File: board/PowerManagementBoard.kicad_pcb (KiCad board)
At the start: 2 copper layers, 168 parts, among them IC1 ACS37010LLZATR-030B3, IC2 ACS37010LLZATR-030B3, IC3 ACS37010LLZATR-030B3, IC4 ACS37010LLZATR-030B3, IC5 ACS37010LLZATR-030B3, IC6 ACS37010LLZATR-030B3, J1 RJ45_LED_Shielded, J10 768250002, J11 768250002, J12 768250002, J2 SS-73100-082, J3 SS-73100-082, J4 SS-73100-082, J5 768250002, J6 768250002, J7 768250002, J8 768250002, J9 768250002, Q1 BSS138, Q10 Si4162DY, Q2 IPB180N10S4-02, Q3 Si4162DY, Q4 IPB180N10S4-02, Q5 Si4162DY, Q6 Si4162DY, Q7 Si4162DY, Q8 Si4162DY, Q9 IPB180N10S4-02, U1 LT1910, U10 ACS72981LLRATR-100U3, U11 LT1910, U12 LT1910, U13 LT1910, U14 LT1910, U15 Teensy4.1_DEV-16771, U16 OKI-78SR-3.3_1.5-W36H-C, U17 OKI-78SR-5_1.5-W36H-C, U18 Opamp_Dual, U19 LT1910, U2 LM5050MK-1_NOPB, U20 LT1910, U3 LM5050MK-1_NOPB, U4 Opamp_Dual, U5 Opamp_Dual, U6 Opamp_Dual

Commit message: PCB start
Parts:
- moved Conn2 36.0 mm to (76.1, 168.5)
- moved Q2 27.7 mm to (95.0, 162.6)
- moved J5 6.38 mm to (20.9, 128.0)
- moved J10 6.38 mm to (64.8, 102.2)
- moved J12 6.38 mm to (86.8, 102.2)
- moved J6 6.38 mm to (20.9, 102.2)
- moved J9 6.38 mm to (53.8, 102.2)
- moved J7 6.38 mm to (31.9, 102.2)
- moved J8 6.38 mm to (42.9, 102.2)
- moved J11 6.38 mm to (75.8, 102.2)
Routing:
- net /TeensyandEthernetCircuit/LED: track 0.00 -> 79.8 mm

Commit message: designated an area for each circuit on pcb
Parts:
- removed the U5 at (122.9, 29.5)
- moved R51 258.9 mm to (67.7, 167.2)
- moved R52 258.9 mm to (67.7, 169.8)
- moved R53 257.6 mm to (44.3, 129.5), turned to 90 degrees
- moved R54 255.5 mm to (46.3, 131.3), turned to -90 degrees
- moved C17 255.4 mm to (44.1, 141.6)
- moved R49 255.1 mm to (44.1, 139.8)
- moved R50 251.7 mm to (47.0, 140.7), turned to -90 degrees
- moved C23 249.7 mm to (43.3, 132.2)
- moved D2 247.1 mm to (44.7, 190.3)
- moved D3 247.1 mm to (44.7, 194.9)
- moved Q9 246.1 mm to (51.4, 181.9)
- moved C18 246.0 mm to (67.7, 164.7)
- moved U3 240.6 mm to (60.2, 190.3)
- moved V3 238.5 mm to (22.5, 185.4), turned to 90 degrees
- moved R42 237.4 mm to (91.8, 168.9)
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- renumbered U18 to U5
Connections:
- net /Anderson/Cam1 renamed /LC
- U5 pad 4: (no net) -> GND
- U5 pad 5: (no net) -> Net-(U5B-+)
- U5 pad 6: (no net) -> Net-(U5B--)
- U5 pad 7: (no net) -> Net-(R22-Pad1)
- U5 pad 8: (no net) -> +24V
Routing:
- net /TeensyandEthernetCircuit/RX+: track 58.3 -> 99.6 mm
- net /TeensyandEthernetCircuit/TX+: track 60.6 -> 101.5 mm
- net /TeensyandEthernetCircuit/RX-: track 61.0 -> 95.8 mm
- net /TeensyandEthernetCircuit/TX-: track 67.5 -> 101.9 mm
- net /TeensyandEthernetCircuit/LED: track 79.8 -> 114.1 mm
- net GND: track 0.00 -> 17.6 mm
- net Net-(D4-K): track 0.00 -> 16.6 mm
- net Net-(IC1-VREF): track 0.00 -> 6.29 mm
- net +3V3: track 0.00 -> 1.86 mm
- added copper zone on F.Cu, net /LC

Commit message: Configuration of parts
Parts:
- moved R27 83.1 mm to (192.8, 108.4), turned to 180 degrees
- moved D6 63.3 mm to (188.8, 108.6)
- moved R11 39.4 mm to (206.2, 137.7)
- moved R10 37.6 mm to (211.7, 133.6), turned to 0 degrees
- moved U6 36.2 mm to (201.5, 133.0), turned to 0 degrees
- moved R19 33.4 mm to (219.9, 112.2), turned to 0 degrees
- moved R9 31.2 mm to (219.8, 117.1), turned to 0 degrees
- moved IC6 30.5 mm to (51.3, 147.3), turned to 180 degrees
- moved R52 29.1 mm to (45.7, 150.7), turned to -90 degrees
- moved R24 26.6 mm to (219.8, 104.6), turned to 0 degrees
- moved R12 25.1 mm to (206.1, 132.8)
- moved D8 25.0 mm to (181.7, 105.4), turned to 180 degrees
- moved R51 24.7 mm to (49.2, 150.9), turned to 180 degrees
- moved R13 21.3 mm to (201.5, 129.1), turned to 0 degrees
- moved U5 21.3 mm to (198.4, 118.3), turned to 0 degrees
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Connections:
- R3 pad 1: +3.3V -> +3V3
- R35 pad 1: +3.3V -> +3V3
- R36 pad 1: +3.3V -> +3V3
- R37 pad 1: +3.3V -> +3V3
- R38 pad 1: +3.3V -> +3V3
- R44 pad 1: +3.3V -> +3V3
- R45 pad 1: +3.3V -> +3V3
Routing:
- net +3V3: track 1.86 -> 86.8 mm
- net +5V: track 0.00 -> 8.00 mm
- net Net-(IC6-VREF): track 0.00 -> 4.79 mm
- net Net-(D23-A): track 0.00 -> 2.55 mm
- net Net-(D22-A): track 0.00 -> 2.55 mm
- net Net-(U13-FAULT): track 0.00 -> 2.52 mm
- net Net-(D18-A): track 0.00 -> 2.45 mm

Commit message: Rearrangement #2
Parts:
- added C13: 1000uF, Capacitor_THT:CP_Radial_D16.0mm_P7.50mm, F.Cu at (40.4, 25.9)
- added C24: 1000uF, Capacitor_THT:CP_Radial_D16.0mm_P7.50mm, F.Cu at (22.6, 48.3)
- added C4: 1000uF, Capacitor_THT:CP_Radial_D16.0mm_P7.50mm, F.Cu at (40.6, 47.6)
- Conn1: footprint MRDT_Connectors:MOLEX_SL_07_Horizontal -> MRDT_Connectors:MOLEX_SL_07_Vertical
- moved Conn1 157.4 mm to (72.2, 67.1), turned to 0 degrees
- moved R24 150.5 mm to (72.3, 74.9), turned to 90 degrees
- moved R4 148.6 mm to (74.9, 74.8), turned to 90 degrees
- moved R14 146.6 mm to (77.5, 74.8), turned to 90 degrees
- moved R19 144.9 mm to (79.9, 74.8), turned to 90 degrees
- moved R30 143.0 mm to (82.5, 74.9), turned to 90 degrees
- moved Conn2 142.7 mm to (135.5, 52.6), turned to -90 degrees
- moved R9 141.5 mm to (84.8, 74.9), turned to 90 degrees
- moved R16 137.9 mm to (70.8, 87.0), turned to 90 degrees
- moved R15 136.4 mm to (72.5, 87.0), turned to 90 degrees
- moved R18 134.8 mm to (74.3, 87.1), turned to 90 degrees
- moved R56 134.5 mm to (124.1, 61.8), turned to -90 degrees
- moved LCD1 134.4 mm to (93.0, 98.4), turned to 180 degrees
- moved R17 131.9 mm to (73.3, 90.4), turned to 180 degrees
- moved C9 131.4 mm to (15.4, 140.8), turned to 180 degrees
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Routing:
- net /TeensyandEthernetCircuit/LED: track 114.1 -> 0.00 mm
- net /TeensyandEthernetCircuit/TX-: track 101.9 -> 0.00 mm
- net /TeensyandEthernetCircuit/TX+: track 101.5 -> 0.00 mm
- net /TeensyandEthernetCircuit/RX+: track 99.6 -> 0.00 mm
- net /TeensyandEthernetCircuit/RX-: track 95.8 -> 0.00 mm
- net +3V3: track 86.8 -> 0.07 mm
- net Net-(D4-K): track 16.6 -> 0.00 mm
- net Net-(C9-Pad1): track 15.3 -> 0.00 mm
- net +5V: track 8.00 -> 0.07 mm
- net Net-(IC1-VREF): track 6.29 -> 0.00 mm
- net Net-(IC6-VREF): track 4.79 -> 0.00 mm
- net Net-(D22-A): track 2.55 -> 0.01 mm
- net Net-(D23-A): track 2.55 -> 0.01 mm
- net Net-(D18-A): track 2.45 -> 0.00 mm

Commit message: Board before M5 Kill
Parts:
- removed Conn2: AndersonPP, MRDT_Connectors:Square_Anderson_2_H_Side_By_Side_PV
- added J13: 768250002, PowerManagementBoard:CONN_SD-76825-0100_02_MOL, F.Cu at (179.4, 40.3)
- added J14: 768250002, PowerManagementBoard:CONN_SD-76825-0100_02_MOL, F.Cu at (168.4, 40.3)
- added J15: 768250002, PowerManagementBoard:CONN_SD-76825-0100_02_MOL, F.Cu at (157.4, 40.3)
- added J16: 768250002, PowerManagementBoard:CONN_SD-76825-0100_02_MOL, F.Cu at (72.3, 40.7)
- added J17: 768250002, PowerManagementBoard:CONN_SD-76825-0100_02_MOL, F.Cu at (61.3, 40.7)
- added J18: 768250002, PowerManagementBoard:CONN_SD-76825-0100_02_MOL, F.Cu at (50.3, 40.7)
- moved H1 231.0 mm to (197.8, 150.7)
- moved H4 196.2 mm to (198.2, 36.6)
- moved J7 182.5 mm to (190.1, 58.6), turned to 90 degrees
- moved J5 181.4 mm to (190.0, 48.6), turned to 90 degrees
- moved R49 172.5 mm to (183.3, 55.2), turned to 180 degrees
- moved C17 172.3 mm to (183.3, 53.4), turned to 180 degrees
- moved R50 168.3 mm to (180.4, 54.3), turned to 90 degrees
- moved D1 165.6 mm to (193.7, 139.8)
- moved Q1 165.6 mm to (192.9, 142.9)
- moved R34 165.6 mm to (193.6, 137.8)
- moved B1 165.6 mm to (185.6, 135.1)
- moved IC3 164.5 mm to (177.3, 58.7), turned to 0 degrees
- moved C9 162.1 mm to (177.0, 128.0), turned to -90 degrees
- moved R37 162.0 mm to (178.9, 48.6), turned to 180 degrees
- moved Q5 158.7 mm to (174.5, 53.1), turned to 180 degrees
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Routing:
- net GND: track 17.6 -> 0.07 mm
- net Net-(D2-K): track 0.00 -> 3.62 mm
- net Net-(U13-FAULT): track 2.52 -> 0.08 mm
- net +24V: track 0.00 -> 2.24 mm
- net Net-(Q2-G): vias 0 -> 1
- net /Anderson/Motor: vias 0 -> 5
- added copper zone on F.Cu, net +24V
- added copper zone on B.Cu, net /Anderson/Motor
- added copper zone on F.Cu, net GND
- added copper zone on F.Cu, net Net-(D14-K)

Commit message: Planned layout - before wiring.
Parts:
- removed C16: 0.1uF, Capacitor_SMD:C_0603_1608Metric_Pad1.08x0.95mm_HandSolder
- removed C22: 10uF, Capacitor_SMD:C_0603_1608Metric_Pad1.08x0.95mm_HandSolder
- removed D17, D19: GRN, LED_SMD:LED_0603_1608Metric_Pad1.05x0.95mm_HandSolder
- removed IC5: ACS37010LLZATR-030B3, PowerManagementBoard:IC_ACS37030LLZATR-040B3
- removed J4: SS-73100-082, PowerManagementBoard:BEL_SS-73100-082
- removed Q10: Si4162DY, Package_SO:SOIC-8_3.9x4.9mm_P1.27mm
- removed R45: 5.1k, Resistor_SMD:R_0603_1608Metric_Pad0.98x0.95mm_HandSolder
- removed R47, R48: 10k, Resistor_SMD:R_0603_1608Metric_Pad0.98x0.95mm_HandSolder
- removed R57, R59: 6.8k, Resistor_SMD:R_0603_1608Metric_Pad0.98x0.95mm_HandSolder
- removed U20: LT1910, Package_SO:SOIC-8_3.9x4.9mm_P1.27mm
- moved C26 95.0 mm to (87.9, 141.8)
- moved C25 95.0 mm to (85.4, 141.8)
- moved D23 95.0 mm to (92.9, 141.8)
- moved R63 95.0 mm to (90.4, 141.8)
- moved U17 95.0 mm to (86.6, 123.8)
- moved U12 79.1 mm to (92.9, 53.1)
- moved R36 78.9 mm to (93.6, 59.1)
- moved R60 78.9 mm to (86.7, 59.5)
- moved C6 78.3 mm to (92.9, 48.4)
- moved D20 78.1 mm to (89.3, 59.5)
- moved Q7 75.7 mm to (86.2, 53.1), turned to 90 degrees
- moved C19 73.9 mm to (99.0, 142.0)
- moved C20 73.9 mm to (101.5, 142.0)
- moved D22 73.9 mm to (105.9, 141.9)
- moved U16 73.9 mm to (99.6, 123.6)
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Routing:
- net Net-(D14-K): track 0.00 -> 40.7 mm
- net Net-(D2-K): track 3.62 -> 0.00 mm
- net +24V: track 2.24 -> 0.00 mm
- net Net-(Q2-G): vias 1 -> 0
- added copper zone on B.Cu, net GND
- added copper zone on F.Cu, net Net-(D2-K)
- added copper zone on F.Cu, net Net-(D4-K)

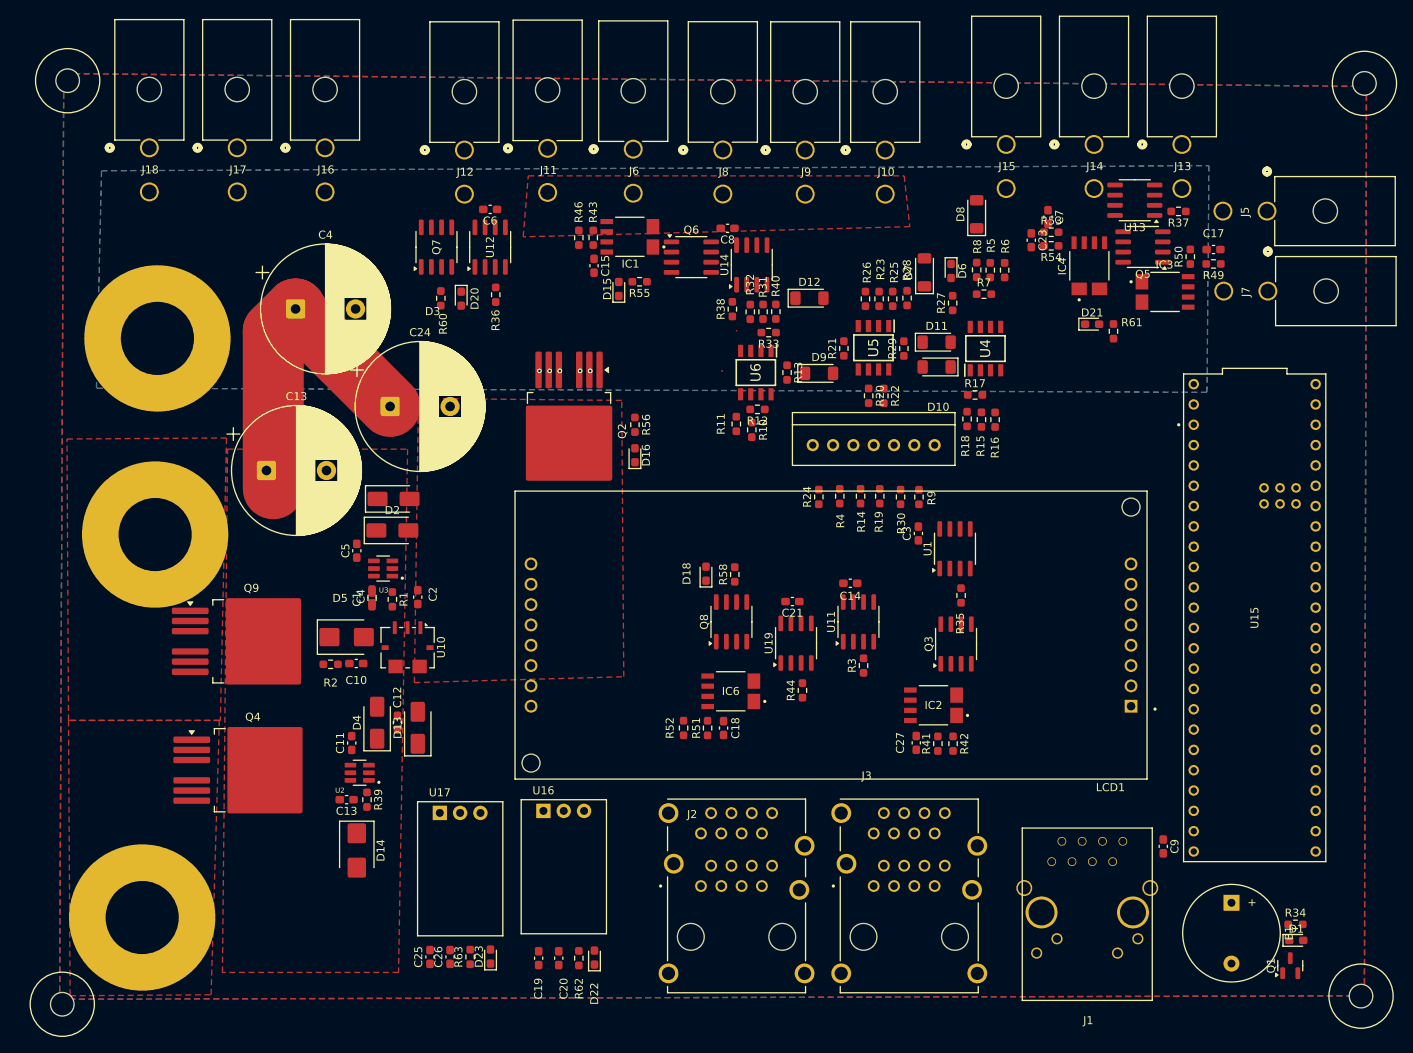
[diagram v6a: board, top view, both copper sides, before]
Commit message: added edge cuts
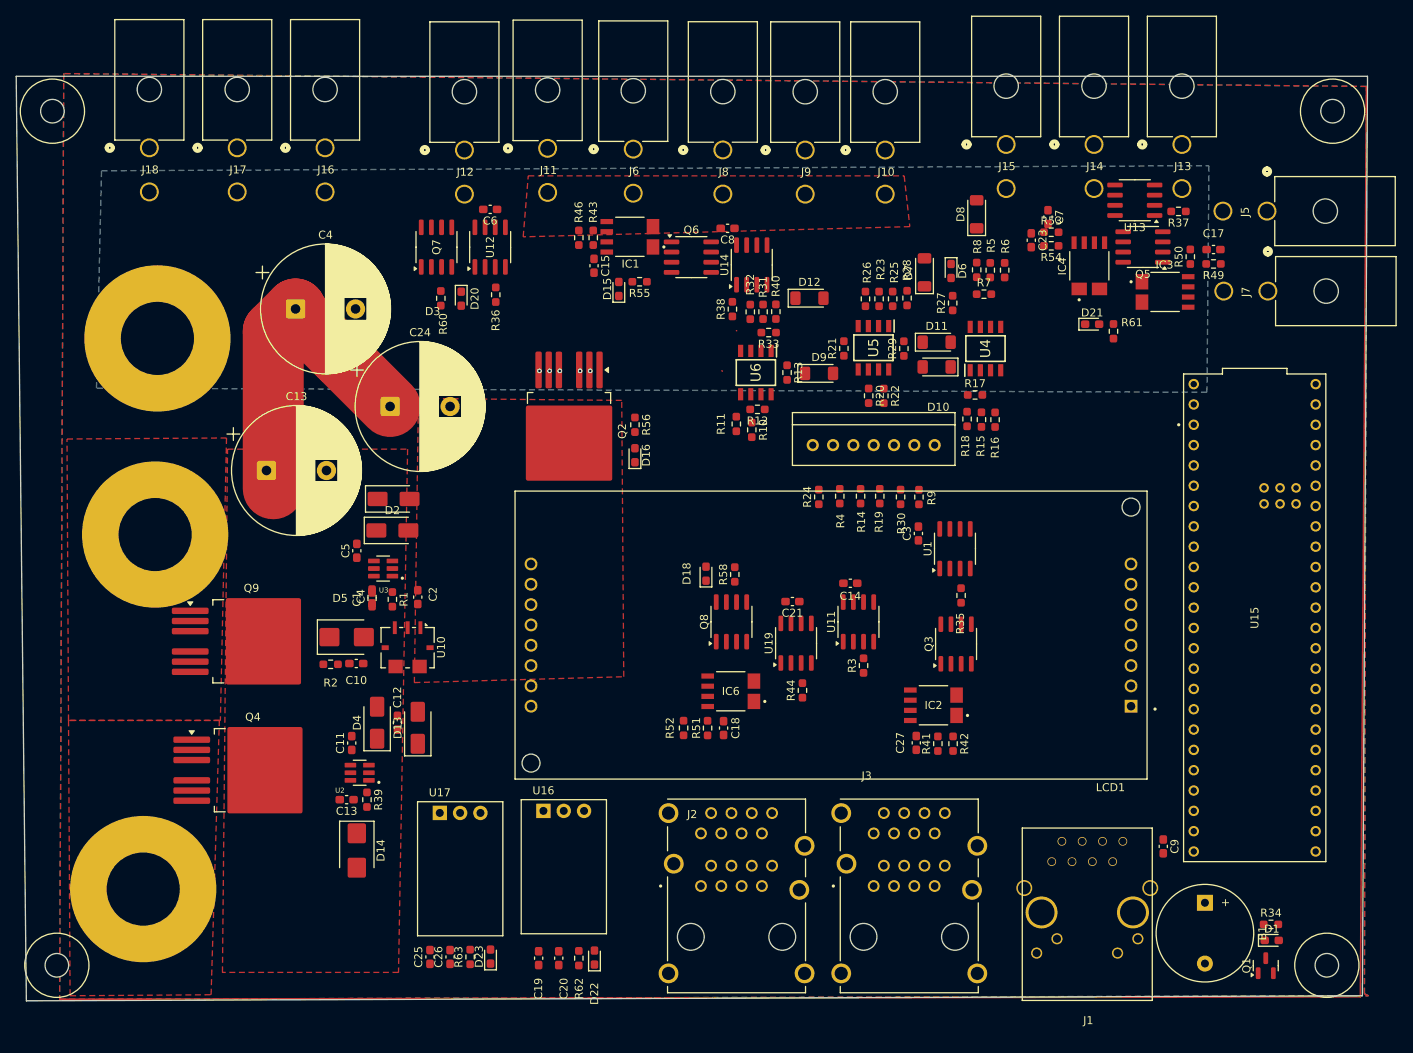
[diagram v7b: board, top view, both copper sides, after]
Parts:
- moved H1 5.75 mm to (193.5, 146.9)
- moved H4 5.28 mm to (194.2, 40.1)
- moved H2 4.92 mm to (42.7, 146.9)
- moved H3 4.26 mm to (34.2, 40.1)
- moved V1 3.56 mm to (49.5, 133.3)
- moved B1 3.32 mm to (182.2, 135.1)
- moved D1 3.06 mm to (190.6, 139.8)
- moved Q1 3.06 mm to (189.8, 142.9)
- moved R34 3.06 mm to (190.5, 137.8)
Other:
- board outline added: 168.9 x 115.6 mm
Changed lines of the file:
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@@
 	(footprint "Resistor_SMD:R_0603_1608Metric_Pad0.98x0.95mm_HandSolder"
 		(layer "F.Cu")
-		(at 193.563 137.761)
+		(at 190.5 137.761)
 		(descr "Resistor SMD 0603 (1608 Metric), square (rectangular) end terminal, IPC-7351 nominal with elongated pad for handsoldering. (Body size source: IPC-SM-782 page 72, https://www.pcb-3d.com/wordpress/wp-content/uploads/ipc-sm-782a_amendment_1_and_2.pdf), generated with kicad-footprint-generator")
 		(tags "resistor handsolder")
@@
 	(footprint "MRDT_Drill_Holes:4_40_Hole_Corner"
 		(layer "F.Cu")
-		(at 197.7503 150.7377)
+		(at 193.47688 146.88312)
 		(property "Reference" "H1"
 			(at 4.00812 -3.50812 0)
@@
 	(footprint "MRDT_Drill_Holes:4_40_Hole_Corner"
 		(layer "F.Cu")
-		(at 36.0793 36.3107)
+		(at 34.1743 40.1207)
 		(property "Reference" "H3"
 			(at 4.00812 -3.50812 0)
@@
 	(footprint "LED_SMD:LED_0603_1608Metric_Pad1.05x0.95mm_HandSolder"
 		(layer "F.Cu")
-		(at 193.663 139.761)
+		(at 190.6 139.761)
 		(descr "LED SMD 0603 (1608 Metric), square (rectangular) end terminal, IPC-7351 nominal, (Body size source: http://www.tortai-tech.com/upload/download/2011102023233369053.pdf), generated with kicad-footprint-generator")
 		(tags "LED handsolder")
@@
 	(footprint "Package_TO_SOT_SMD:SOT-23"
 		(layer "F.Cu")
-		(at 192.913 142.9235 90)
+		(at 189.85 142.9235 90)
 		(descr "SOT, 3 Pin (JEDEC TO-236 Var AB https://www.jedec.org/document_search?search_api_views_fulltext=TO-236), generated with kicad-footprint-generator ipc_gullwing_generator.py")
 		(tags "SOT TO_SOT_SMD")
@@
 	(footprint "MRDT_Drill_Holes:4_40_Hole_Corner"
 		(layer "F.Cu")
-		(at 43.4227 151.7537 90)
+		(at 42.74312 146.88312 90)
 		(property "Reference" "H2"
 			(at 4.00812 -3.50812 90)
@@
 	(footprint "Buzzer_Beeper:Buzzer_12x9.5RM7.6"
 		(layer "F.Cu")
-		(at 185.563 135.061 -90)
+		(at 182.245 135.061 -90)
 		(descr "Generic Buzzer, D12mm height 9.5mm with RM7.6mm")
 		(tags "buzzer")
@@
 	(footprint "MRDT_Drill_Holes:BATT_PWR_VIA"
 		(layer "F.Cu")
-		(at 49.403 136.906 180)
+		(at 49.53 133.35 180)
 		(property "Reference" "V1"
 			(at 0 10.16 0)
@@
 	(footprint "MRDT_Drill_Holes:4_40_Hole_Corner"
 		(layer "F.Cu")
-		(at 198.17588 36.64712)
+		(at 194.1943 40.1207)
 		(property "Reference" "H4"
 			(at 4.00812 -3.50812 0)
@@
 		)
 	)
+	(gr_line
+		(start 202.438 33.02)
+		(end 201.676 146.812)
+		(stroke
+			(width 0.2)
+			(type default)
+		)
+		(layer "F.Cu")
+	)
+	(gr_line
+		(start 201.676 146.812)
+		(end 39.087387 147.123226)
+		(stroke
+			(width 0.2)
+			(type default)
+		)
+		(layer "F.Cu")
+	)
+	(gr_line
+		(start 33.655 31.75)
+		(end 202.565 31.75)
+		(stroke
+			(width 0.05)
+			(type default)
+		)
+		(layer "Edge.Cuts")
+	)
+	(gr_line
+		(start 34.925 147.32)
+		(end 33.655 31.75)
+		(stroke
+			(width 0.05)
+			(type default)
+		)
+		(layer "Edge.Cuts")
+	)
+	(gr_line
+		(start 202.565 33.02)
+		(end 201.93 146.685)
+		(stroke
+			(width 0.05)
+			(type default)
+		)
+		(layer "Edge.Cuts")
+	)
+	(gr_line
+		(start 201.93 146.685)
+		(end 34.925 147.32)
+		(stroke
+			(width 0.05)
+			(type default)
+		)
+		(layer "Edge.Cuts")
+	)
+	(gr_line
+		(start 202.565 31.75)
+		(end 202.565 33.02)
+		(stroke
+			(width 0.05)
+			(type default)
+		)
+		(layer "Edge.Cuts")
+	)
 	(segment

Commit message: Most Traces done
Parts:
- moved R36 75.3 mm to (168.9, 60.6), turned to 180 degrees
- moved Q7 74.6 mm to (160.8, 55.6)
- moved U12 74.5 mm to (167.4, 55.6)
- moved C6 74.5 mm to (167.4, 50.7)
- moved D20 74.4 mm to (163.7, 60.8), turned to 180 degrees
- moved R60 73.2 mm to (159.9, 60.8), turned to 0 degrees
- moved J12 53.6 mm to (143.3, 40.6)
- moved J11 32.2 mm to (132.3, 40.6)
- moved J18 24.9 mm to (75.2, 40.6)
- moved J8 22.6 mm to (99.4, 40.6)
- moved C23 22.4 mm to (138.2, 50.5)
- moved J6 22.4 mm to (88.4, 40.6)
- moved J13 22.4 mm to (157.0, 40.6)
- moved R53 22.4 mm to (140.7, 49.5)
- moved R54 22.4 mm to (140.7, 51.2)
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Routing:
- net +3V3: track 0.00 -> 340.9 mm, vias 0 -> 14
- net +5V: track 0.07 -> 183.5 mm, vias 0 -> 1
- net +24V: track 0.00 -> 167.1 mm, vias 0 -> 8
- net /LCD/D6: track 0.00 -> 153.2 mm, vias 0 -> 1
- net /LCD/D7: track 0.00 -> 137.8 mm, vias 0 -> 1
- net /Current Protection/BattVout: track 0.00 -> 133.9 mm, vias 0 -> 3
- net /Switching Circuit/LC_EN: track 0.00 -> 112.7 mm, vias 0 -> 2
- net /LCD/D3: track 0.00 -> 111.9 mm, vias 0 -> 2
- net /LCD/D2: track 0.00 -> 100.0 mm, vias 0 -> 2
- net /LCD/D5: track 0.00 -> 99.4 mm, vias 0 -> 3
- net /LCD/D4: track 0.00 -> 95.4 mm, vias 0 -> 1
- net /Switching Circuit/M2_EN: track 0.00 -> 62.8 mm, vias 0 -> 2
- net Net-(Q2-G): track 0.00 -> 61.9 mm, vias 0 -> 2
- net Net-(Conn1-Pad3): track 0.00 -> 48.8 mm, vias 0 -> 2
- net Net-(U4B-+): track 0.00 -> 48.8 mm, vias 0 -> 2
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- added copper zone on F.Cu, net /Current-Sensinator/LCin
- added copper zone on F.Cu, net /Current-Sensinator/m2in
- added copper zone on B.Cu, net /Current-Sensinator/m2out
- added copper zone on B.Cu, net Net-(D14-K)
- added copper zone on B.Cu, net Net-(D2-K)
- added copper zone on B.Cu, net Net-(D4-K)
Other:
- board size 168.9 x 115.6 mm -> 167.9 x 115.3 mm
